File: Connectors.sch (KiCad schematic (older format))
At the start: 4 parts

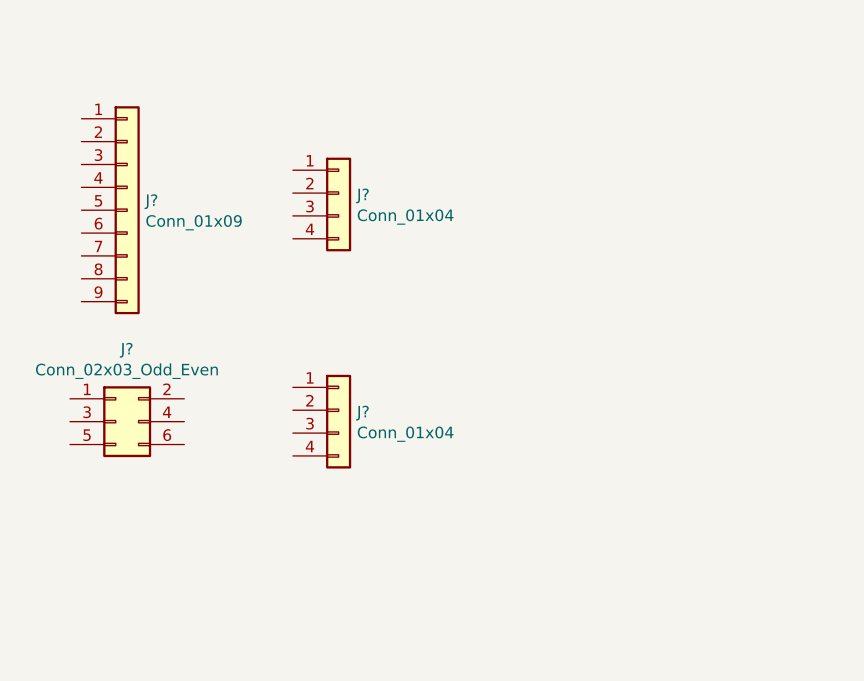
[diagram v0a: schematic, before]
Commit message: Arrenged symbols.
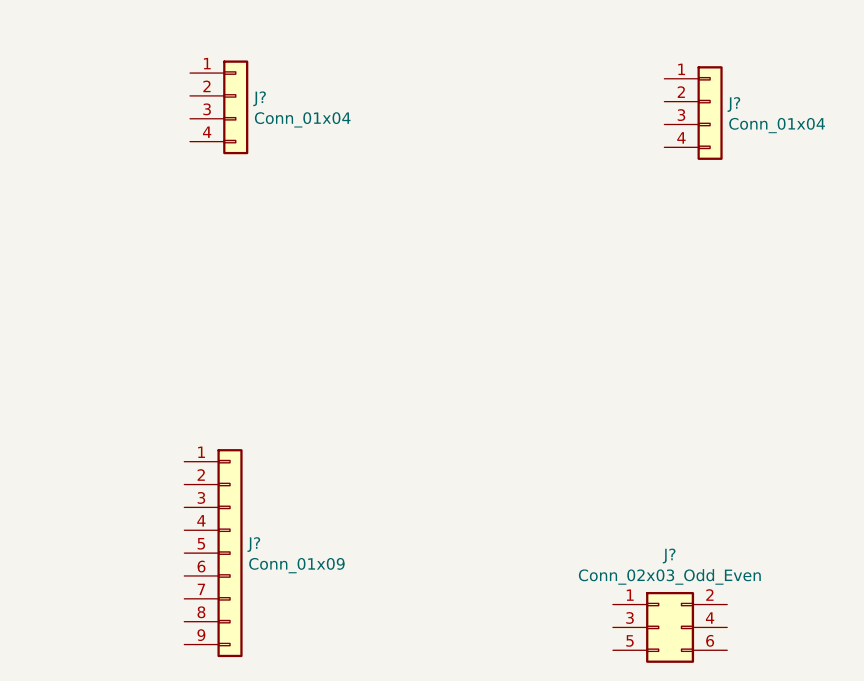
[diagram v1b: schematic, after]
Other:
- moved on the sheet: J?
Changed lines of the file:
@@
 L Connector_Generic:Conn_01x09 J?
 U 1 1 5F0D3D13
-P 4350 3250
-F 0 "J?" H 4430 3292 50  0000 L CNN
-F 1 "Conn_01x09" H 4430 3201 50  0000 L CNN
-F 2 "" H 4350 3250 50  0001 C CNN
-F 3 "~" H 4350 3250 50  0001 C CNN
-	1    4350 3250
+P 4800 4750
+F 0 "J?" H 4880 4792 50  0000 L CNN
+F 1 "Conn_01x09" H 4880 4701 50  0000 L CNN
+F 2 "" H 4800 4750 50  0001 C CNN
+F 3 "~" H 4800 4750 50  0001 C CNN
+	1    4800 4750
 	1    0    0    -1
 $EndComp
@@
 L Connector_Generic:Conn_01x04 J?
 U 1 1 5F0D4D1E
-P 5275 3175
-F 0 "J?" H 5355 3167 50  0000 L CNN
-F 1 "Conn_01x04" H 5355 3076 50  0000 L CNN
-F 2 "" H 5275 3175 50  0001 C CNN
-F 3 "~" H 5275 3175 50  0001 C CNN
-	1    5275 3175
+P 4825 2750
+F 0 "J?" H 4905 2742 50  0000 L CNN
+F 1 "Conn_01x04" H 4905 2651 50  0000 L CNN
+F 2 "" H 4825 2750 50  0001 C CNN
+F 3 "~" H 4825 2750 50  0001 C CNN
+	1    4825 2750
 	1    0    0    -1
 $EndComp
@@
 L Connector_Generic:Conn_02x03_Odd_Even J?
 U 1 1 5F0D5455
-P 4300 4175
-F 0 "J?" H 4350 4492 50  0000 C CNN
-F 1 "Conn_02x03_Odd_Even" H 4350 4401 50  0000 C CNN
-F 2 "" H 4300 4175 50  0001 C CNN
-F 3 "~" H 4300 4175 50  0001 C CNN
-	1    4300 4175
+P 6675 5075
+F 0 "J?" H 6725 5392 50  0000 C CNN
+F 1 "Conn_02x03_Odd_Even" H 6725 5301 50  0000 C CNN
+F 2 "" H 6675 5075 50  0001 C CNN
+F 3 "~" H 6675 5075 50  0001 C CNN
+	1    6675 5075
 	1    0    0    -1
 $EndComp
@@
 L Connector_Generic:Conn_01x04 J?
 U 1 1 5F0D5F3F
-P 5275 4125
-F 0 "J?" H 5355 4117 50  0000 L CNN
-F 1 "Conn_01x04" H 5355 4026 50  0000 L CNN
-F 2 "" H 5275 4125 50  0001 C CNN
-F 3 "~" H 5275 4125 50  0001 C CNN
-	1    5275 4125
+P 6900 2775
+F 0 "J?" H 6980 2767 50  0000 L CNN
+F 1 "Conn_01x04" H 6980 2676 50  0000 L CNN
+F 2 "" H 6900 2775 50  0001 C CNN
+F 3 "~" H 6900 2775 50  0001 C CNN
+	1    6900 2775
 	1    0    0    -1
 $EndComp

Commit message: Annotated.
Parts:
- gave numbers to parts that had none: 4
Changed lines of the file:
@@
 $EndDescr
 $Comp
-L Connector_Generic:Conn_01x09 J?
+L Connector_Generic:Conn_01x09 J1
 U 1 1 5F0D3D13
 P 4800 4750
-F 0 "J?" H 4880 4792 50  0000 L CNN
+F 0 "J1" H 4880 4792 50  0000 L CNN
 F 1 "Conn_01x09" H 4880 4701 50  0000 L CNN
 F 2 "" H 4800 4750 50  0001 C CNN
@@
 $EndComp
 $Comp
-L Connector_Generic:Conn_01x04 J?
+L Connector_Generic:Conn_01x04 J2
 U 1 1 5F0D4D1E
 P 4825 2750
-F 0 "J?" H 4905 2742 50  0000 L CNN
+F 0 "J2" H 4905 2742 50  0000 L CNN
 F 1 "Conn_01x04" H 4905 2651 50  0000 L CNN
 F 2 "" H 4825 2750 50  0001 C CNN
@@
 $EndComp
 $Comp
-L Connector_Generic:Conn_02x03_Odd_Even J?
+L Connector_Generic:Conn_02x03_Odd_Even J3
 U 1 1 5F0D5455
 P 6675 5075
-F 0 "J?" H 6725 5392 50  0000 C CNN
+F 0 "J3" H 6725 5392 50  0000 C CNN
 F 1 "Conn_02x03_Odd_Even" H 6725 5301 50  0000 C CNN
 F 2 "" H 6675 5075 50  0001 C CNN
@@
 $EndComp
 $Comp
-L Connector_Generic:Conn_01x04 J?
+L Connector_Generic:Conn_01x04 J4
 U 1 1 5F0D5F3F
 P 6900 2775
-F 0 "J?" H 6980 2767 50  0000 L CNN
+F 0 "J4" H 6980 2767 50  0000 L CNN
 F 1 "Conn_01x04" H 6980 2676 50  0000 L CNN
 F 2 "" H 6900 2775 50  0001 C CNN

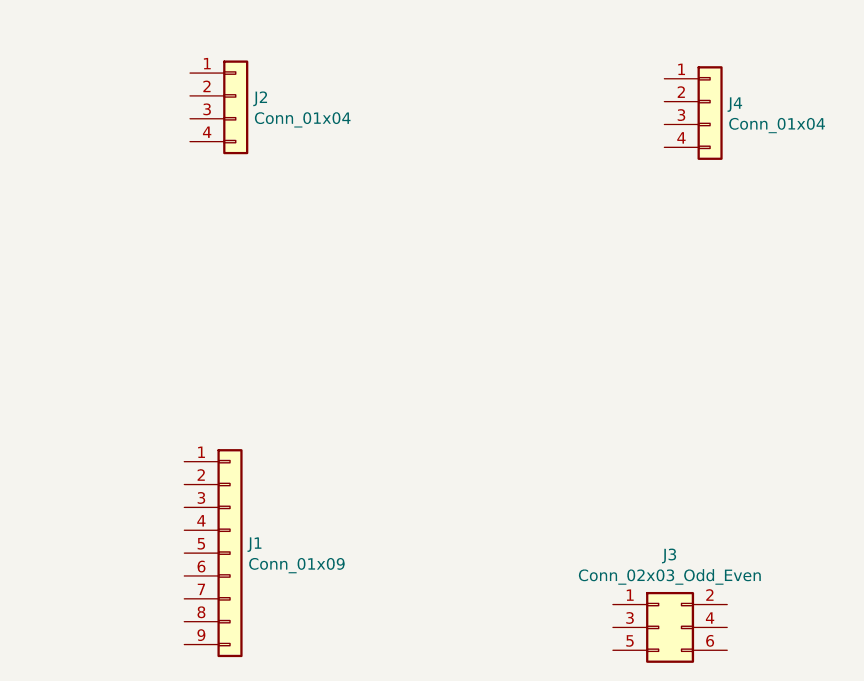
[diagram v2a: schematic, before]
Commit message: Completed association and added component values.
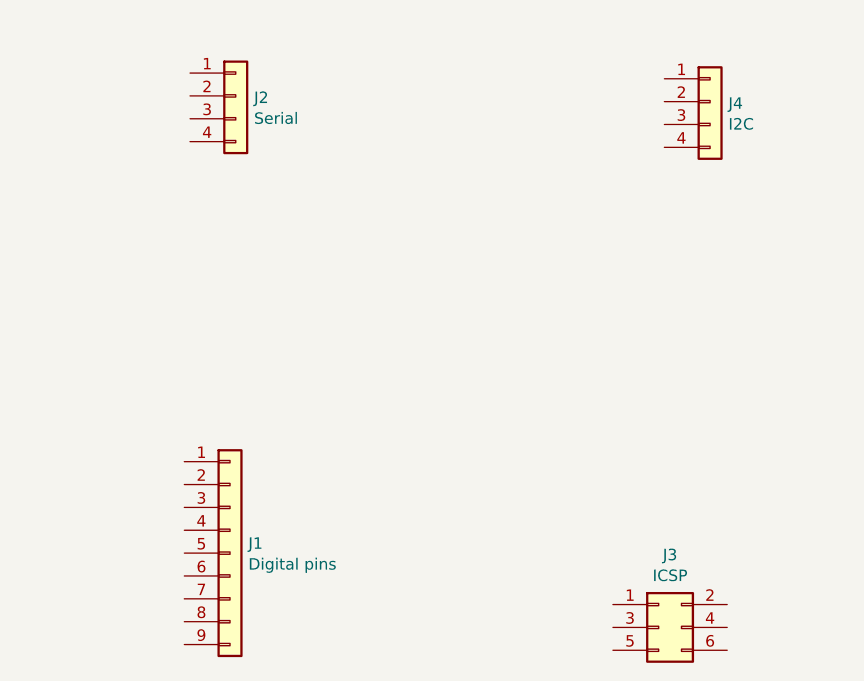
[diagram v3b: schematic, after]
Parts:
- J1: value Conn_01x09 -> Digital pins; footprint (none) -> Connector_PinSocket_2.54mm:PinSocket_1x09_P2.54mm_Vertical
- J2: value Conn_01x04 -> Serial; footprint (none) -> Connector_PinSocket_2.54mm:PinSocket_1x04_P2.54mm_Vertical
- J3: value Conn_02x03_Odd_Even -> ICSP; footprint (none) -> Connector_PinSocket_2.54mm:PinSocket_2x03_P2.54mm_Vertical
- J4: value Conn_01x04 -> I2C; footprint (none) -> Connector_PinSocket_2.54mm:PinSocket_1x04_P2.54mm_Vertical
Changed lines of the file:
@@
 P 4800 4750
 F 0 "J1" H 4880 4792 50  0000 L CNN
-F 1 "Conn_01x09" H 4880 4701 50  0000 L CNN
-F 2 "" H 4800 4750 50  0001 C CNN
+F 1 "Digital pins" H 4880 4701 50  0000 L CNN
+F 2 "Connector_PinSocket_2.54mm:PinSocket_1x09_P2.54mm_Vertical" H 4800 4750 50  0001 C CNN
 F 3 "~" H 4800 4750 50  0001 C CNN
 	1    4800 4750
@@
 P 4825 2750
 F 0 "J2" H 4905 2742 50  0000 L CNN
-F 1 "Conn_01x04" H 4905 2651 50  0000 L CNN
-F 2 "" H 4825 2750 50  0001 C CNN
+F 1 "Serial" H 4905 2651 50  0000 L CNN
+F 2 "Connector_PinSocket_2.54mm:PinSocket_1x04_P2.54mm_Vertical" H 4825 2750 50  0001 C CNN
 F 3 "~" H 4825 2750 50  0001 C CNN
 	1    4825 2750
@@
 P 6675 5075
 F 0 "J3" H 6725 5392 50  0000 C CNN
-F 1 "Conn_02x03_Odd_Even" H 6725 5301 50  0000 C CNN
-F 2 "" H 6675 5075 50  0001 C CNN
+F 1 "ICSP" H 6725 5301 50  0000 C CNN
+F 2 "Connector_PinSocket_2.54mm:PinSocket_2x03_P2.54mm_Vertical" H 6675 5075 50  0001 C CNN
 F 3 "~" H 6675 5075 50  0001 C CNN
 	1    6675 5075
@@
 P 6900 2775
 F 0 "J4" H 6980 2767 50  0000 L CNN
-F 1 "Conn_01x04" H 6980 2676 50  0000 L CNN
-F 2 "" H 6900 2775 50  0001 C CNN
+F 1 "I2C" H 6980 2676 50  0000 L CNN
+F 2 "Connector_PinSocket_2.54mm:PinSocket_1x04_P2.54mm_Vertical" H 6900 2775 50  0001 C CNN
 F 3 "~" H 6900 2775 50  0001 C CNN
 	1    6900 2775

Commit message: Completed wiring in connectors sheet
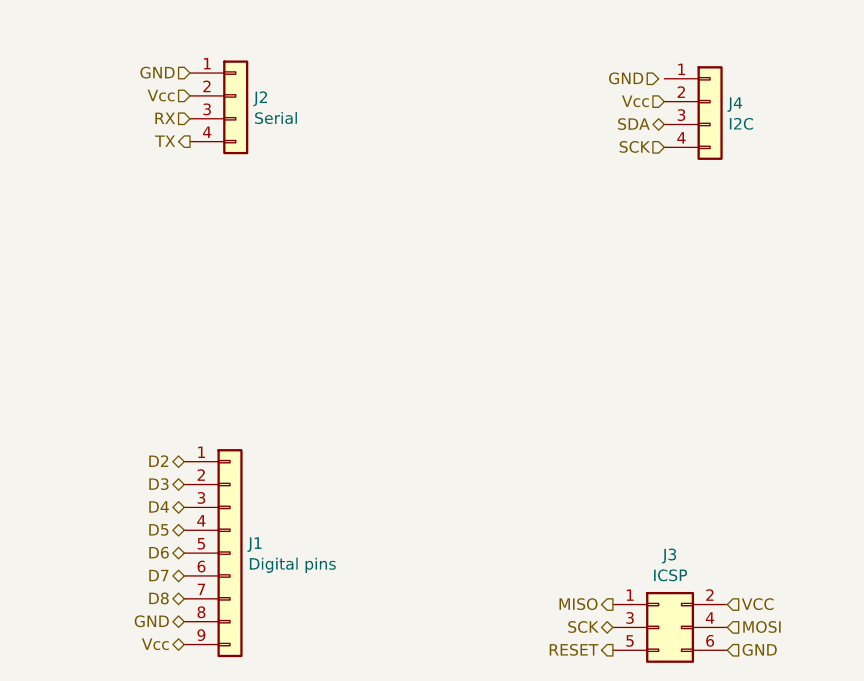
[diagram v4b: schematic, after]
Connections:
- net D2: now reaches J1.1 (Pin_1)
- net D3: now reaches J1.2 (Pin_2)
- net D4: now reaches J1.3 (Pin_3)
- net D5: now reaches J1.4 (Pin_4)
- net D6: now reaches J1.5 (Pin_5)
- net D7: now reaches J1.6 (Pin_6)
- net D8: now reaches J1.7 (Pin_7)
- net GND: now reaches J1.8 (Pin_8)
- net GND: now also J2.1 (Pin_1), J3.6 (Pin_6)
- net Vcc: now reaches J1.9 (Pin_9)
- net Vcc: now also J2.2 (Pin_2), J4.2 (Pin_2)
- net RX: now reaches J2.3 (Pin_3)
- net TX: now reaches J2.4 (Pin_4)
- net MISO: now reaches J3.1 (Pin_1)
- net VCC: now reaches J3.2 (Pin_2)
- net SCK: now reaches J3.3 (Pin_3)
- net SCK: now also J4.4 (Pin_4)
- net MOSI: now reaches J3.4 (Pin_4)
- net RESET: now reaches J3.5 (Pin_5)
- net SDA: now reaches J4.3 (Pin_3)
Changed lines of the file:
@@
 	1    0    0    -1
 $EndComp
+Text HLabel 6475 4975 0    50   Output ~ 0
+MISO
+Text HLabel 6475 5075 0    50   BiDi ~ 0
+SCK
+Text HLabel 6475 5175 0    50   Output ~ 0
+RESET
+Text HLabel 6975 4975 2    50   Input ~ 0
+VCC
+Text HLabel 6975 5075 2    50   Input ~ 0
+MOSI
+Text HLabel 6975 5175 2    50   Input ~ 0
+GND
+Text HLabel 4625 2650 0    50   Input ~ 0
+GND
+Text HLabel 4625 2750 0    50   Input ~ 0
+Vcc
+Text HLabel 4625 2850 0    50   Input ~ 0
+RX
+Text HLabel 4625 2950 0    50   Output ~ 0
+TX
+Text HLabel 6675 2675 0    50   Input ~ 0
+GND
+Text HLabel 6700 2775 0    50   Input ~ 0
+Vcc
+Text HLabel 6700 2975 0    50   Input ~ 0
+SCK
+Text HLabel 6700 2875 0    50   BiDi ~ 0
+SDA
+Text HLabel 4600 4350 0    50   BiDi ~ 0
+D2
+Text HLabel 4600 4450 0    50   BiDi ~ 0
+D3
+Text HLabel 4600 4550 0    50   BiDi ~ 0
+D4
+Text HLabel 4600 4650 0    50   BiDi ~ 0
+D5
+Text HLabel 4600 4750 0    50   BiDi ~ 0
+D6
+Text HLabel 4600 4850 0    50   BiDi ~ 0
+D7
+Text HLabel 4600 4950 0    50   BiDi ~ 0
+D8
+Text HLabel 4600 5050 0    50   BiDi ~ 0
+GND
+Text HLabel 4600 5150 0    50   BiDi ~ 0
+Vcc
 $EndSCHEMATC

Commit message: Added power flag symbol.
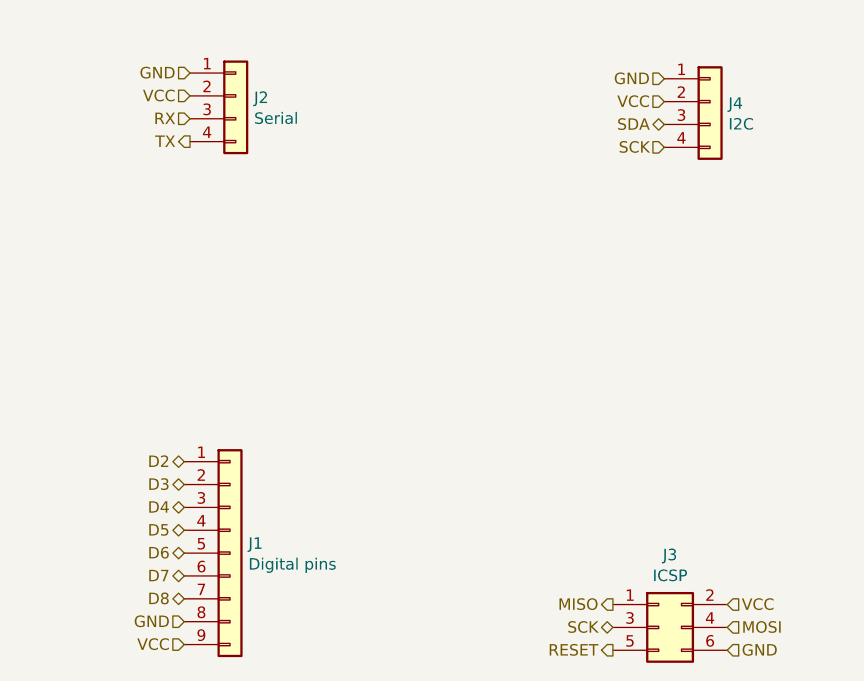
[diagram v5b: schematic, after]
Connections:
- net Vcc is gone; now on net VCC: J1.9 (Pin_9), J2.2 (Pin_2), J4.2 (Pin_2)
- net GND: now also J4.1 (Pin_1)
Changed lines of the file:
@@
 GND
 Text HLabel 4625 2750 0    50   Input ~ 0
-Vcc
+VCC
 Text HLabel 4625 2850 0    50   Input ~ 0
 RX
 Text HLabel 4625 2950 0    50   Output ~ 0
 TX
-Text HLabel 6675 2675 0    50   Input ~ 0
+Text HLabel 6700 2675 0    50   Input ~ 0
 GND
 Text HLabel 6700 2775 0    50   Input ~ 0
-Vcc
+VCC
 Text HLabel 6700 2975 0    50   Input ~ 0
 SCK
@@
 Text HLabel 4600 4950 0    50   BiDi ~ 0
 D8
-Text HLabel 4600 5050 0    50   BiDi ~ 0
+Text HLabel 4600 5050 0    50   Input ~ 0
 GND
-Text HLabel 4600 5150 0    50   BiDi ~ 0
-Vcc
+Text HLabel 4600 5150 0    50   Input ~ 0
+VCC
 $EndSCHEMATC

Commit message: Added functional block descriptions.
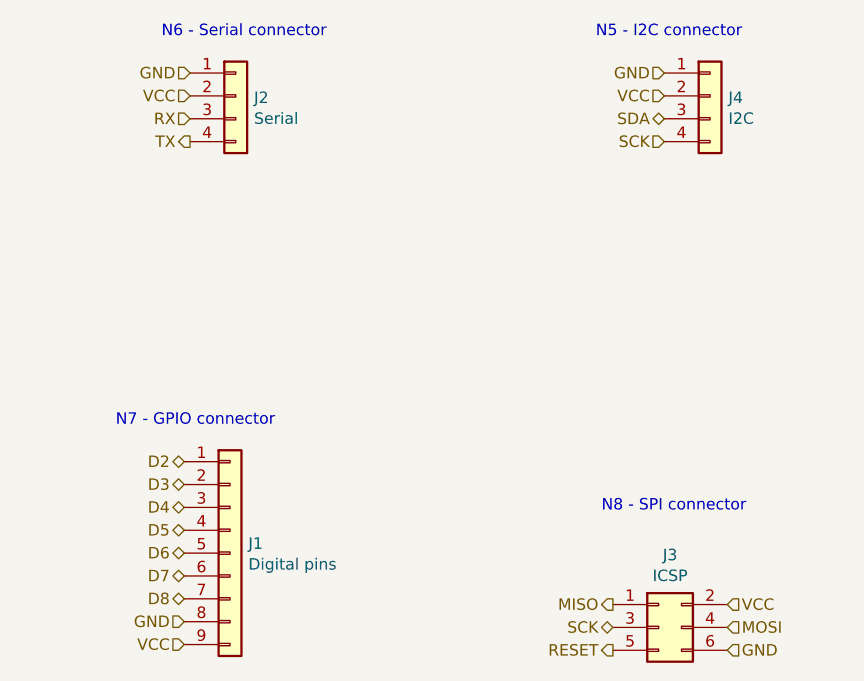
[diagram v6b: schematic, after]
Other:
- note added: "N5 - I2C connector\n"
- note added: "N6 - Serial connector"
- note added: "N7 - GPIO connector"
- note added: "N8 - SPI connector"
- moved on the sheet: J4
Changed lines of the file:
@@
 L Connector_Generic:Conn_01x04 J4
 U 1 1 5F0D5F3F
-P 6900 2775
-F 0 "J4" H 6980 2767 50  0000 L CNN
-F 1 "I2C" H 6980 2676 50  0000 L CNN
-F 2 "Connector_PinSocket_2.54mm:PinSocket_1x04_P2.54mm_Vertical" H 6900 2775 50  0001 C CNN
-F 3 "~" H 6900 2775 50  0001 C CNN
-	1    6900 2775
+P 6900 2750
+F 0 "J4" H 6980 2742 50  0000 L CNN
+F 1 "I2C" H 6980 2651 50  0000 L CNN
+F 2 "Connector_PinSocket_2.54mm:PinSocket_1x04_P2.54mm_Vertical" H 6900 2750 50  0001 C CNN
+F 3 "~" H 6900 2750 50  0001 C CNN
+	1    6900 2750
 	1    0    0    -1
 $EndComp
@@
 Text HLabel 4625 2950 0    50   Output ~ 0
 TX
-Text HLabel 6700 2675 0    50   Input ~ 0
+Text HLabel 6700 2650 0    50   Input ~ 0
 GND
-Text HLabel 6700 2775 0    50   Input ~ 0
+Text HLabel 6700 2750 0    50   Input ~ 0
 VCC
-Text HLabel 6700 2975 0    50   Input ~ 0
+Text HLabel 6700 2950 0    50   Input ~ 0
 SCK
-Text HLabel 6700 2875 0    50   BiDi ~ 0
+Text HLabel 6700 2850 0    50   BiDi ~ 0
 SDA
 Text HLabel 4600 4350 0    50   BiDi ~ 0
@@
 Text HLabel 4600 5150 0    50   Input ~ 0
 VCC
+Text Notes 4500 2500 0    50   ~ 0
+N6 - Serial connector
+Text Notes 6400 2500 0    50   ~ 0
+N5 - I2C connector\n
+Text Notes 4300 4200 0    50   ~ 0
+N7 - GPIO connector
+Text Notes 6425 4575 0    50   ~ 0
+N8 - SPI connector
 $EndSCHEMATC
